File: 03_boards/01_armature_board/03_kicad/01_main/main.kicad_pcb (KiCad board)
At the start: 2 copper layers, 4 parts, among them U1 STM32G431K8Tx, U2 LD1117S33, U3 MAX3485, U4 ADXL343

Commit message: Updated armature board footprints
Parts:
- added C1: 1uf, Capacitor_SMD:C_0603_1608Metric, F.Cu at (228.5, 76.3)
- added C10: 10nf, Capacitor_SMD:C_0603_1608Metric, F.Cu at (228.5, 88.9)
- added C11: 30pf, Capacitor_SMD:C_0603_1608Metric, F.Cu at (228.5, 91.4)
- added C12: 30pf, Capacitor_SMD:C_0603_1608Metric, F.Cu at (232.5, 76.3)
- added C13: 100nf, Capacitor_SMD:C_0603_1608Metric, F.Cu at (232.5, 78.8)
- added C14: 100nf, Capacitor_SMD:C_0603_1608Metric, F.Cu at (232.5, 81.3)
- added C15: 100nf, Capacitor_SMD:C_0603_1608Metric, F.Cu at (232.5, 83.8)
- added C16: 10nf, Capacitor_SMD:C_0603_1608Metric, F.Cu at (232.5, 86.3)
- added C17: 10nf, Capacitor_SMD:C_0603_1608Metric, F.Cu at (232.5, 88.9)
- added C18: 10nf, Capacitor_SMD:C_0603_1608Metric, F.Cu at (232.5, 91.4)
- added C19: 10nf, Capacitor_SMD:C_0603_1608Metric, F.Cu at (236.5, 76.3)
- added C20: 10nf, Capacitor_SMD:C_0603_1608Metric, F.Cu at (236.5, 78.8)
- added C21: 10nf, Capacitor_SMD:C_0603_1608Metric, F.Cu at (236.5, 81.3)
- added C22: 10nf, Capacitor_SMD:C_0603_1608Metric, F.Cu at (236.5, 83.8)
- added C23: 10nf, Capacitor_SMD:C_0603_1608Metric, F.Cu at (236.5, 86.3)
- added C3: 100nf, Capacitor_SMD:C_0603_1608Metric, F.Cu at (228.5, 78.8)
- added C4: 10uF, Capacitor_SMD:C_1206_3216Metric, F.Cu at (241.3, 76.7)
- added C5: 100nf, Capacitor_SMD:C_0603_1608Metric, F.Cu at (228.5, 81.3)
- added C6: 1uf, Capacitor_SMD:C_0603_1608Metric, F.Cu at (228.5, 83.8)
- added C7: 10uf, Capacitor_SMD:C_1206_3216Metric, F.Cu at (241.3, 80.1)
- added C8: 22uf, Capacitor_SMD:C_1206_3216Metric, F.Cu at (241.3, 83.4)
- added C9: 100nf, Capacitor_SMD:C_0603_1608Metric, F.Cu at (228.5, 86.3)
- added D1: LED, LED_SMD:LED_1206_3216Metric, F.Cu at (241.3, 86.8)
- added FB1: BLM18AG601SN1D, BLM18AG601SN1D:BEADC1608X95N, F.Cu at (240.5, 89.8)
- added J1: 01x04, Connector_JST:JST_PH_B4B-PH-K_1x04_P2.00mm_Vertical, F.Cu at (229.4, 104.9)
- added J10: 01x02, Connector_JST:JST_PH_B2B-PH-K_1x02_P2.00mm_Vertical, F.Cu at (221.5, 101.0)
- added J11: 01x02, Connector_JST:JST_PH_B2B-PH-K_1x02_P2.00mm_Vertical, F.Cu at (221.5, 107.5)
- added J2: 01x06, Connector_JST:JST_PH_B6B-PH-K_1x06_P2.00mm_Vertical, F.Cu at (235.7, 70.8)
- added J3: 01x05, Connector_JST:JST_PH_B5B-PH-K_1x05_P2.00mm_Vertical, F.Cu at (234.7, 97.9)
- added J4: 01x02, Connector_JST:JST_PH_B2B-PH-K_1x02_P2.00mm_Vertical, F.Cu at (244.8, 105.7)
- added J5: 01x02, Connector_JST:JST_PH_B2B-PH-K_1x02_P2.00mm_Vertical, F.Cu at (221.5, 68.2)
- added J6: 01x02, Connector_JST:JST_PH_B2B-PH-K_1x02_P2.00mm_Vertical, F.Cu at (221.5, 74.8)
- added J7: 01x02, Connector_JST:JST_PH_B2B-PH-K_1x02_P2.00mm_Vertical, F.Cu at (221.5, 81.3)
- added J8: 01x02, Connector_JST:JST_PH_B2B-PH-K_1x02_P2.00mm_Vertical, F.Cu at (221.5, 87.9)
- added J9: 01x02, Connector_JST:JST_PH_B2B-PH-K_1x02_P2.00mm_Vertical, F.Cu at (221.5, 94.4)
- added R1: 10, Resistor_SMD:R_0603_1608Metric, F.Cu at (166.5, 69.8)
- added R10: 1.8k, Resistor_SMD:R_0603_1608Metric, F.Cu at (170.5, 72.3)
- added R11: 1.8k, Resistor_SMD:R_0603_1608Metric, F.Cu at (170.5, 74.8)
- added R12: 1.8k, Resistor_SMD:R_0603_1608Metric, F.Cu at (170.5, 77.3)
- added R13: 1.8k, Resistor_SMD:R_0603_1608Metric, F.Cu at (170.5, 79.8)
- added R14: 1.8k, Resistor_SMD:R_0603_1608Metric, F.Cu at (170.5, 82.3)
- added R15: 1.8k, Resistor_SMD:R_0603_1608Metric, F.Cu at (170.5, 84.8)
- added R16: 220, Resistor_SMD:R_0603_1608Metric, F.Cu at (174.5, 69.8)
- added R17: 220, Resistor_SMD:R_0603_1608Metric, F.Cu at (174.5, 72.3)
- added R18: 0Ω, Resistor_SMD:R_0603_1608Metric, F.Cu at (174.5, 74.8)
- added R19: 0Ω, Resistor_SMD:R_0603_1608Metric, F.Cu at (174.5, 77.3)
- added R2: 10, Resistor_SMD:R_0603_1608Metric, F.Cu at (166.5, 72.3)
- added R3: 120, Resistor_SMD:R_0603_1608Metric, F.Cu at (166.5, 74.8)
- added R5: 10k, Resistor_SMD:R_0603_1608Metric, F.Cu at (166.5, 77.3)
- added R6: 10k, Resistor_SMD:R_0603_1608Metric, F.Cu at (166.5, 79.8)
- added R7: 220, Resistor_SMD:R_0603_1608Metric, F.Cu at (166.5, 82.3)
- added R8: 1.8k, Resistor_SMD:R_0603_1608Metric, F.Cu at (166.5, 84.8)
- added R9: 1.8k, Resistor_SMD:R_0603_1608Metric, F.Cu at (170.5, 69.8)
- added SW1: SW_Push, Button_Switch_THT:SW_PUSH_6mm, F.Cu at (178.6, 70.5)
- added SW2: SW_Push, Button_Switch_THT:SW_PUSH_6mm, F.Cu at (178.6, 79.1)
- added U5: 74HC4051, 74HC4051:SSOP-16, F.Cu at (151.0, 87.0)
- added Y1: ECS-80-20-18-TR, ECS-80-18-23B-JTN-TR:XTAL_ECS-80-20-18-TR, F.Cu at (184.2, 89.4)
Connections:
- U1 pad 30: RS_RC -> RS_TOG

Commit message: Saving pcb layout work for armature board
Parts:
- C16, C17, C18, C19, C20, C21, C22, C23, R10, R11, R12, R13, R14, R15, R8, R9: moved to B.Cu
- PRO1: renamed from J2; footprint Connector_JST:JST_PH_B6B-PH-K_1x06_P2.00mm_Vertical -> Connector_PinHeader_2.54mm:PinHeader_2x03_P2.54mm_Vertical
- SW1, SW2: footprint Button_Switch_THT:SW_PUSH_6mm -> Button_Switch_SMD:SW_Push_1P1T_NO_CK_KMR2
- moved NTC1 250.9 mm to (15.0, 5.00), turned to 180 degrees
- moved C16 233.5 mm to (12.0, 9.37), turned to 180 degrees
- moved INT1 228.4 mm to (12.0, 35.0)
- moved C11 227.5 mm to (11.6, 22.7), turned to 135 degrees
- moved C17 226.9 mm to (20.0, 9.37), turned to 180 degrees
- moved C12 222.8 mm to (15.4, 26.3), turned to 135 degrees
- moved C22 221.3 mm to (28.0, 9.49), turned to 180 degrees
- moved ENC1 219.9 mm to (24.0, 35.0)
- moved R3 218.0 mm to (-25.2, -29.0)
- moved R1 215.0 mm to (-21.8, -34.0)
- moved R7 214.2 mm to (-22.0, -19.4)
- moved R6 213.8 mm to (-21.0, -23.0)
- moved NTC3 213.3 mm to (31.0, 5.00), turned to 180 degrees
- moved C18 212.8 mm to (36.1, 9.42), turned to 180 degrees
- moved R5 212.4 mm to (-18.0, -28.0)
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- renumbered J3 to ENC1, J1 to INT1, J4 to NTC1, J5 to NTC2, J10 to NTC3, J6 to NTC4, J7 to NTC5, J11 to NTC6, J8 to NTC7, J9 to NTC8
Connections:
- C17 pad 1: TA4 -> TA2
- C18 pad 1: TA2 -> TA4
- C20 pad 1: TA3 -> TA7
- C21 pad 1: TA6 -> TA8
- C22 pad 1: TA7 -> TA3
- C23 pad 1: TA8 -> TA6
- NTC2 pad 1: TA4 -> TA2
- NTC3 pad 1: TA7 -> TA3
- NTC4 pad 1: TA2 -> TA4
- NTC6 pad 1: TA8 -> TA6
- NTC7 pad 1: TA3 -> TA7
- NTC8 pad 1: TA6 -> TA8
- R10 pad 2: TA2 -> TA4
- R12 pad 2: TA3 -> TA7
- R13 pad 2: TA6 -> TA8
- R14 pad 2: TA7 -> TA3
- R15 pad 2: TA8 -> TA6
- R9 pad 2: TA4 -> TA2
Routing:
- net TA1: track 0.00 -> 39.0 mm
- net TA2: track 0.00 -> 32.5 mm
- net TA3: track 0.00 -> 25.8 mm
- net TA8: track 0.00 -> 20.8 mm, vias 0 -> 1
- net TA5: track 0.00 -> 19.9 mm, vias 0 -> 1
- net TA6: track 0.00 -> 18.6 mm
- net TA7: track 0.00 -> 18.4 mm
- net TA4: track 0.00 -> 15.7 mm, vias 0 -> 1
- net OSC_IN: track 0.00 -> 14.4 mm
- net OSC_OUT: track 0.00 -> 11.2 mm
- net MPS2: track 0.00 -> 8.16 mm
- net MPS1: track 0.00 -> 7.56 mm
- net MPS0: track 0.00 -> 6.96 mm
- net GND: track 0.00 -> 5.53 mm, vias 0 -> 7
- added copper zone on F.Cu, net +3.3V
- added copper zone on B.Cu, net GND
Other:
- board outline added: 60 x 40 mm

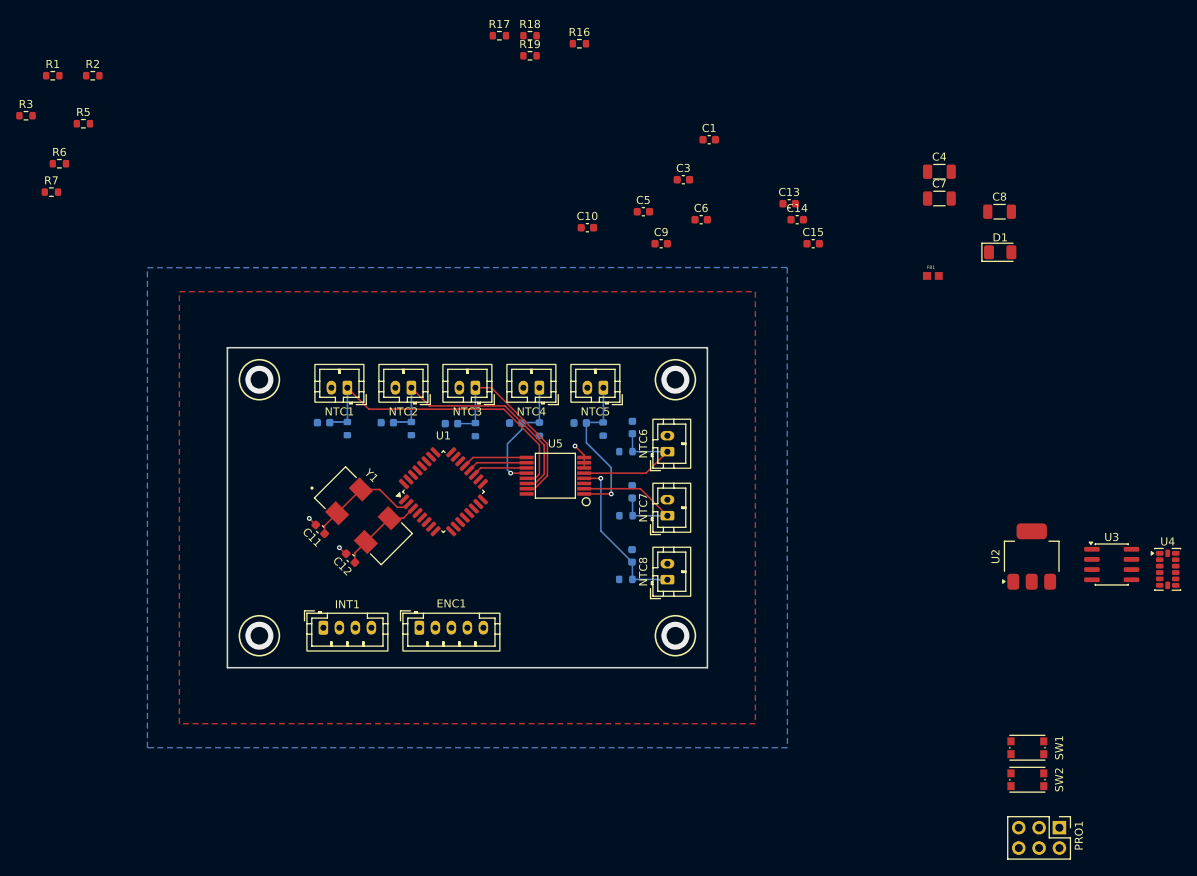
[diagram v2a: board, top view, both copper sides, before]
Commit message: Updates to schematic and nearly finished first schematic draft
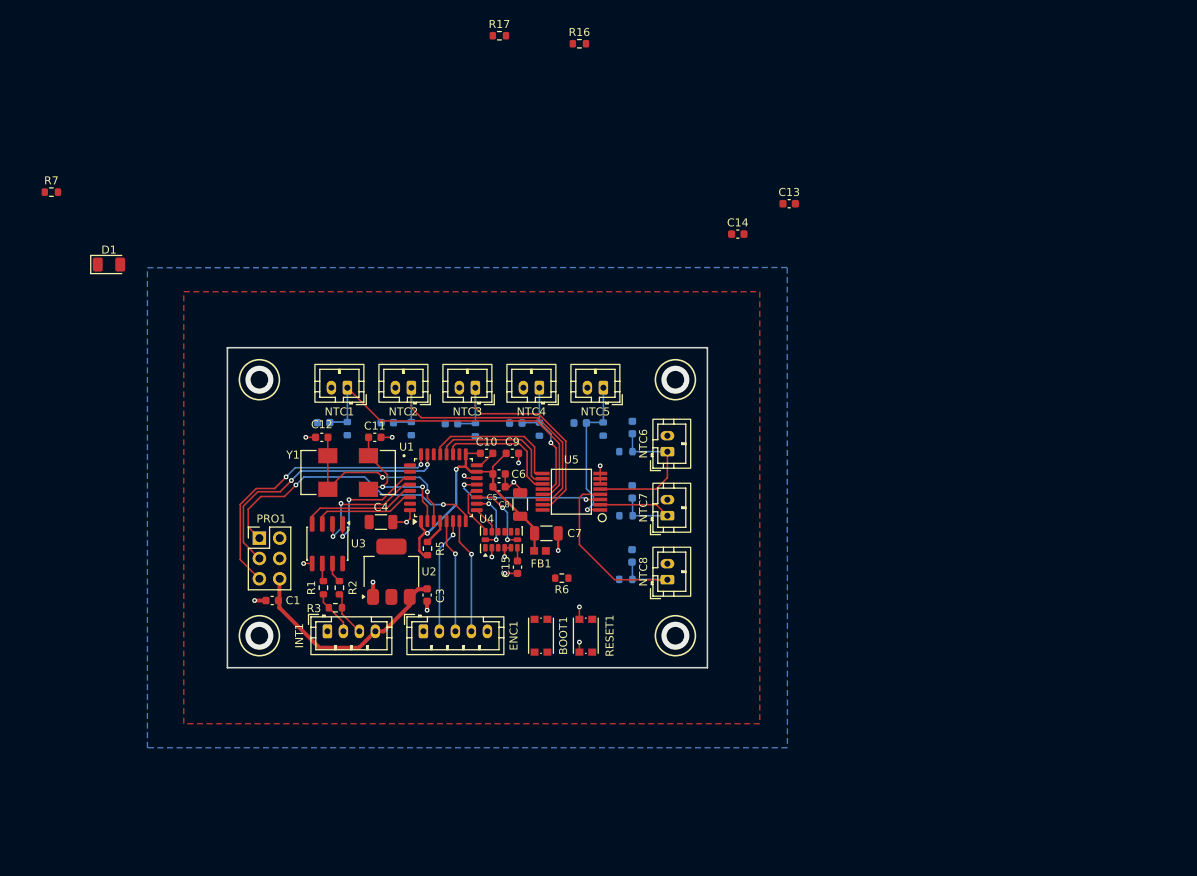
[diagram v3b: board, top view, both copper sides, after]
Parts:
- removed R18, R19: 0Ω, Resistor_SMD:R_0603_1608Metric
- moved D1 111.4 mm to (-14.8, -10.4)
- moved PRO1 106.4 mm to (4.00, 23.8), turned to 0 degrees
- moved U3 98.1 mm to (12.5, 24.5), turned to -90 degrees
- moved U4 83.4 mm to (34.2, 24.0), turned to 90 degrees
- moved C4 82.4 mm to (19.2, 21.8)
- moved R6 81.4 mm to (41.8, 28.8), turned to 180 degrees
- moved U2 80.1 mm to (20.5, 28.0)
- moved C1 79.4 mm to (5.60, 31.6), turned to 180 degrees
- moved R3 72.6 mm to (13.5, 32.5), turned to 180 degrees
- moved R1 72.4 mm to (12.0, 30.0), turned to 90 degrees
- moved R2 71.0 mm to (14.0, 30.0), turned to 90 degrees
- moved C8 70.2 mm to (36.6, 19.6), turned to 90 degrees
- moved R5 68.3 mm to (25.0, 25.1), turned to 90 degrees
- moved C7 64.5 mm to (39.9, 23.2)
- moved BOOT1 62.4 mm to (39.2, 36.0), turned to 90 degrees
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- renumbered SW1 to BOOT1, SW2 to RESET1
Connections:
- INT1 pad 2: RX -> D_P
- INT1 pad 3: TX -> D_N
- R1 pad 1: TX -> D_P
- R2 pad 1: RX -> D_N
- R3 pad 1: RX -> D_N
- R3 pad 2: TX -> D_P
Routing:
- net VDDA: track 0.00 -> 39.2 mm, vias 0 -> 2
- net SWCLK: track 0.00 -> 36.4 mm, vias 0 -> 2
- net SWO: track 0.00 -> 35.8 mm, vias 0 -> 2
- net SWDIO: track 0.00 -> 34.2 mm, vias 0 -> 2
- net GND: track 5.53 -> 34.1 mm, vias 7 -> 21
- net +5V: track 0.00 -> 27.8 mm
- net TA_OUT: track 0.00 -> 19.6 mm, vias 0 -> 2
- net RS_EN: track 0.00 -> 15.9 mm, vias 0 -> 2
- net RS_RC: track 0.00 -> 15.3 mm, vias 0 -> 2
- net RS_DRI: track 0.00 -> 14.5 mm
- net INC_B: track 0.00 -> 14.5 mm, vias 0 -> 1
- net INC_Index: track 0.00 -> 14.4 mm, vias 0 -> 1
- net INC_A: track 0.00 -> 14.2 mm, vias 0 -> 1
- net OSC_OUT: track 11.2 -> 25.3 mm, vias 0 -> 2
- net RS_TOG: track 0.00 -> 12.9 mm
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
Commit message: Finished armature board development. Moving back to encoder board for images etc
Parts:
- C13, C14: moved to B.Cu
- D1: footprint LED_SMD:LED_1206_3216Metric -> LED_SMD:LED_0603_1608Metric_Pad1.05x0.95mm_HandSolder
- moved R17 70.6 mm to (40.1, 31.4), turned to 90 degrees
- moved R16 69.5 mm to (46.4, 31.4), turned to 90 degrees
- moved R7 56.2 mm to (24.9, 11.5), turned to 180 degrees
- moved C13 52.8 mm to (44.6, 28.2), turned to 90 degrees
- moved C14 48.5 mm to (40.2, 28.1), turned to 90 degrees
- moved D1 43.0 mm to (23.0, 10.0)
- moved BOOT1 6.20 mm to (45.4, 36.0), turned to -90 degrees
- moved RESET1 5.80 mm to (39.0, 36.0)
- moved R6 3.82 mm to (44.6, 31.4), turned to 90 degrees
- moved C11 1.62 mm to (16.8, 11.2), turned to 180 degrees
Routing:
- net NRST: track 3.26 -> 58.6 mm, vias 0 -> 5
- net BOOT: track 0.00 -> 43.2 mm, vias 0 -> 3
- net GND: track 34.1 -> 43.3 mm, vias 21 -> 23
- net Net-(R17-Pad1): track 0.00 -> 6.02 mm
- net Net-(BOOT1-Pad1): track 0.00 -> 5.91 mm
- net +3.3V: track 0.00 -> 2.48 mm, vias 0 -> 1
- net Net-(U1-PA12): track 0.00 -> 1.83 mm
- net Net-(D1-A): track 0.00 -> 1.61 mm
- net TA2: track 38.6 -> 38.0 mm
- net INC_Index: vias 1 -> 2
- net INC_B: vias 1 -> 2
- net INC_A: vias 1 -> 2
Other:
- board text added: "Armature Board REV 0"
- board text added: "Wgbowley 26-08-01"
